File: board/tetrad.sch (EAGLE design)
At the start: 92 parts, among them J2 CONN-03X2-MICROFIT-430450612, Q1 FET-PCH-TO252, Q10 FET-NCH-SOT23, Q11 FET-NCH-SOT23, Q12 FET-NCH-SOT23, Q2 FET-NCH-SOT23, Q3 FET-NCH-SOT23, Q4 FET-NCH-SOT23, Q5 FET-NCH-SOT23, Q6 FET-NCH-SOT23, Q7 FET-NCH-SOT23, Q8 FET-NCH-SOT23, Q9 FET-NCH-SOT23, U1 IO-MCP23017SO, U2 RADIO-ESP32_DEVKIT, U3 R-78E5.0-1.0

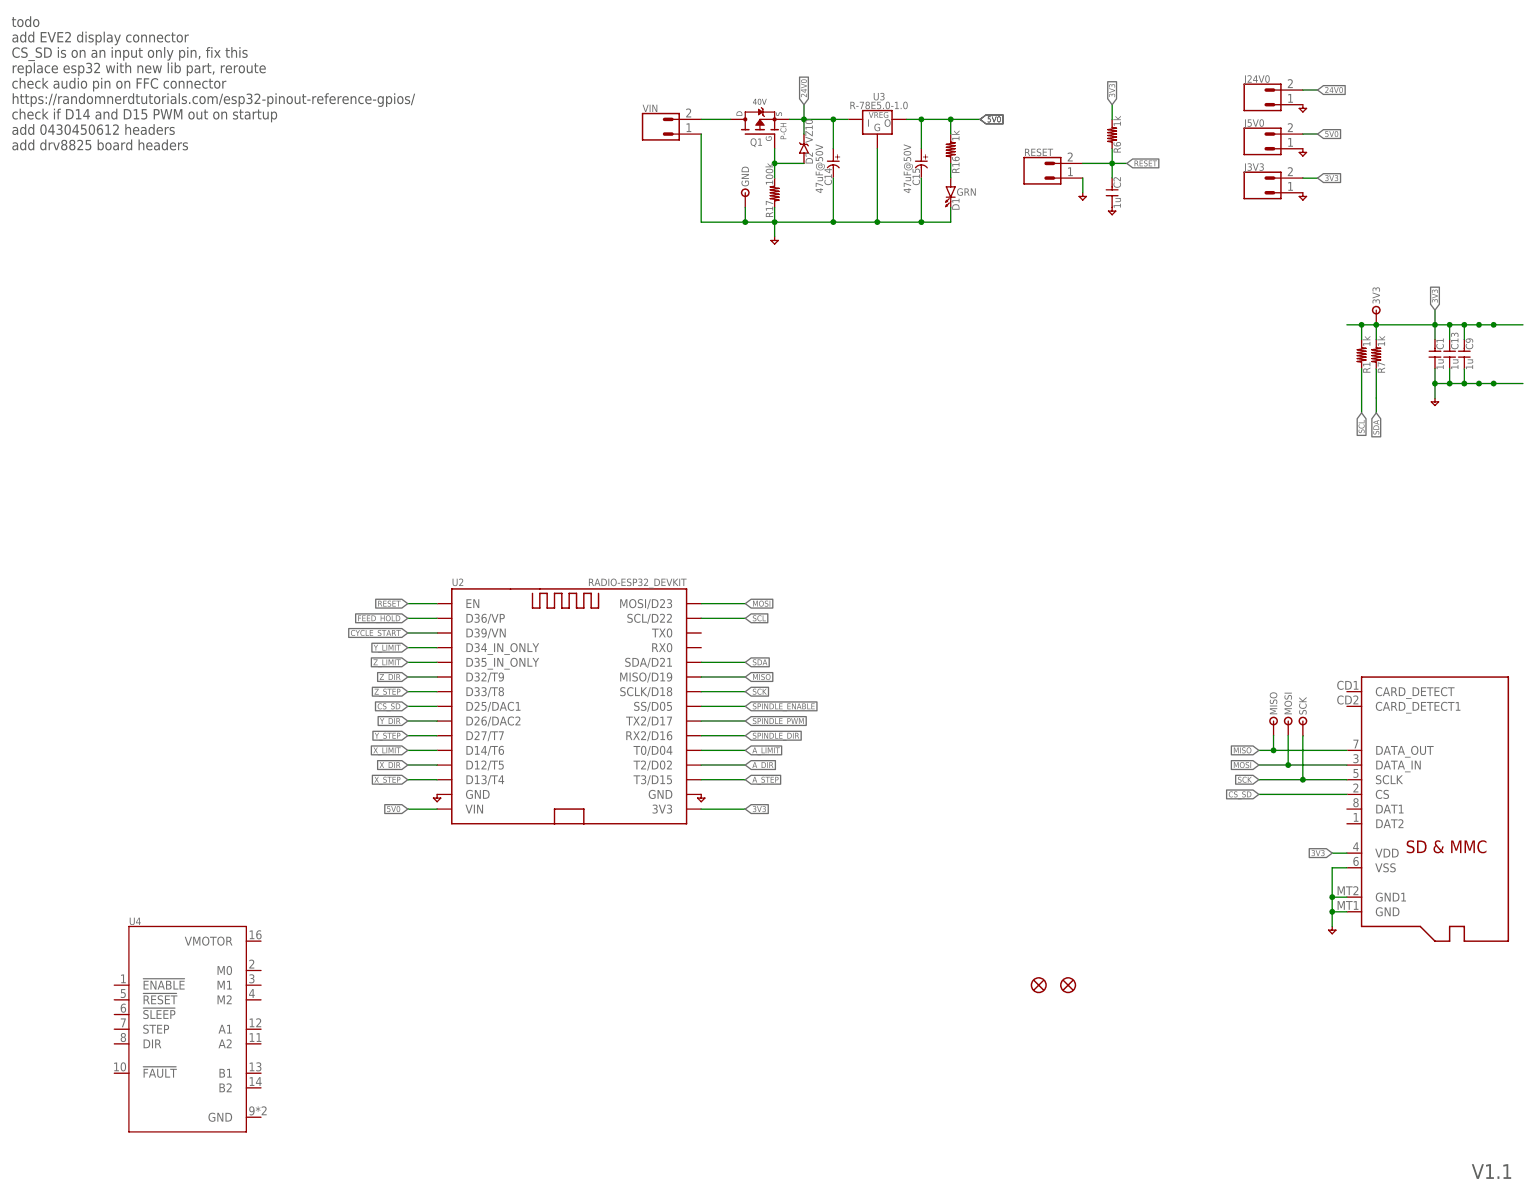
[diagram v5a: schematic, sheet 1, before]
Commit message: selected hammond enclosure and larger board
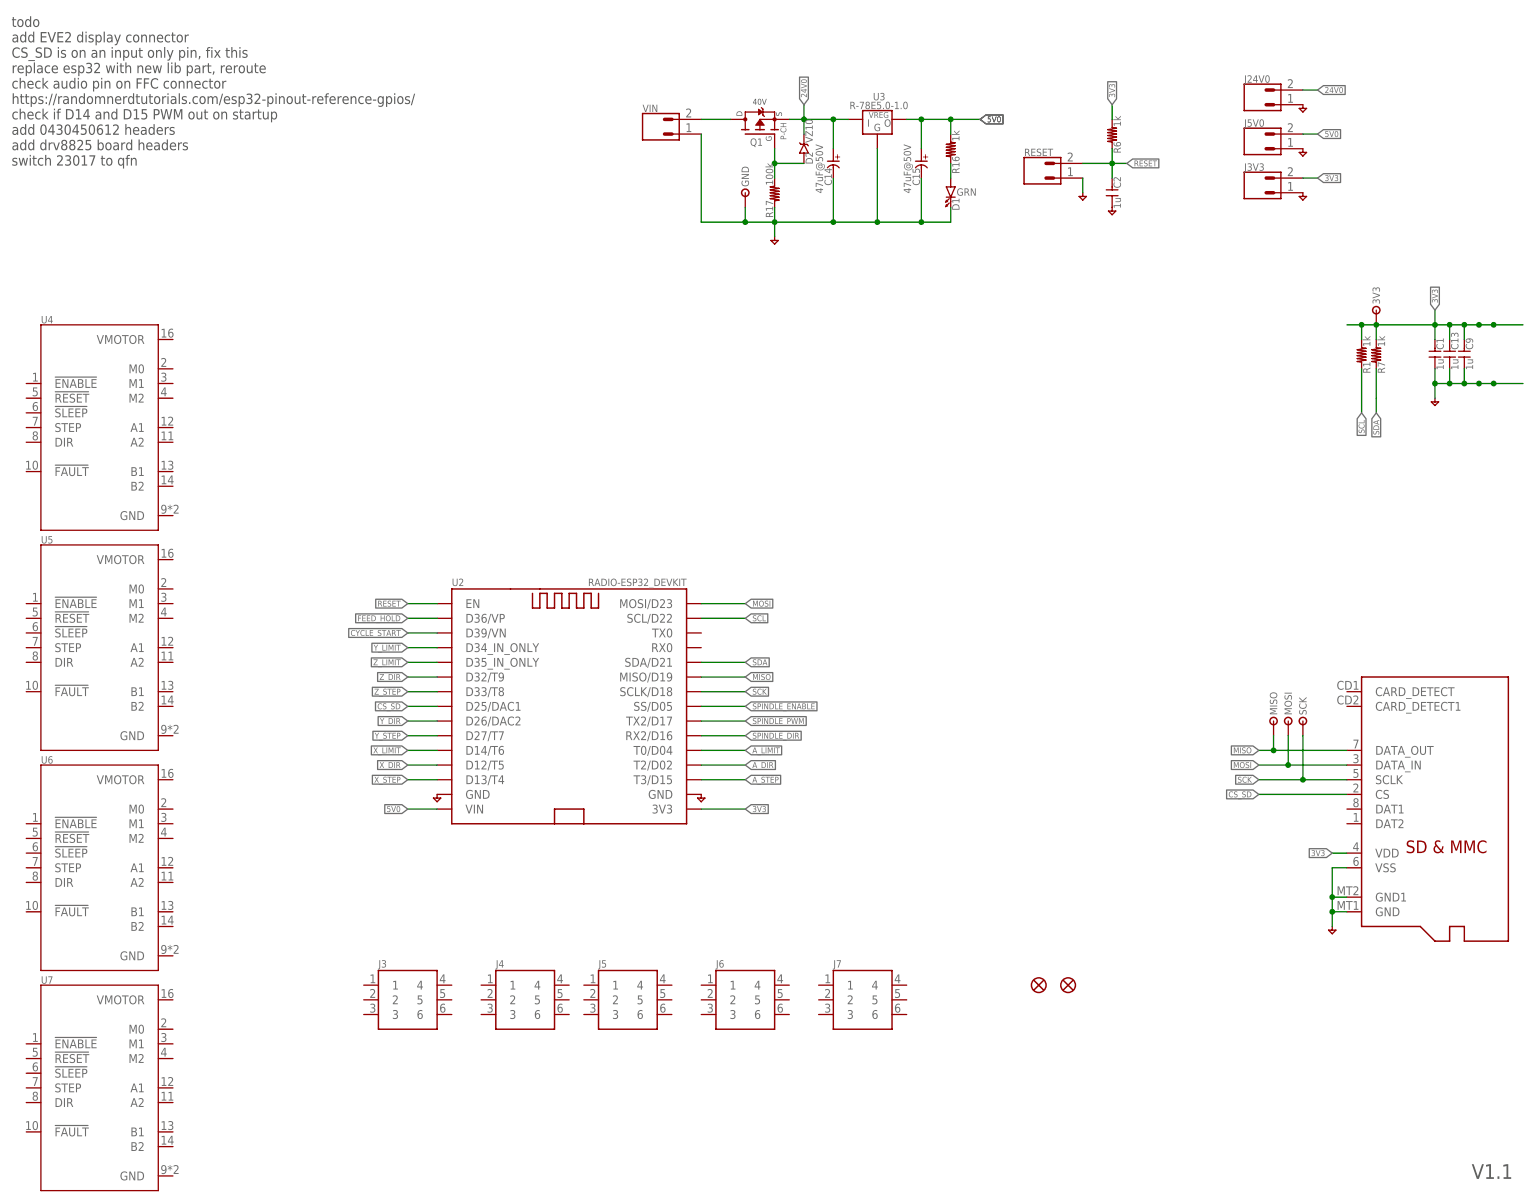
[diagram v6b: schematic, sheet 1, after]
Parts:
- added J3, J4, J5, J6, J7: (no value), holla:CONN-03X2-MICROFIT-430450612
- added U5, U6, U7: (no value), holla:BOARD-DRV8825-CARRIER
- J2: value CONN-03X2-MICROFIT-430450612 -> (none)
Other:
- note added: "todo add EVE2 display connector CS_SD is on an input only pin, fix this replace esp32 with new lib part, reroute check audio pin on FFC connector https://randomnerdtutorials.com/esp32-pinout-reference-gpios/ check if D14 and D15 PWM out on startup add 0430450612 headers add drv8825 board headers switch 23017 to qfn"
- note removed: "todo add EVE2 display connector CS_SD is on an input only pin, fix this replace esp32 with new lib part, reroute check audio pin on FFC connector https://randomnerdtutorials.com/esp32-pinout-reference-gpios/ check if D14 and D15 PWM out on startup add 0430450612 headers add drv8825 board headers"
- moved on the sheet: U4
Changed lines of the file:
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@@
 <part name="J2" library="holla" deviceset="CONN-03X2-MICROFIT" device="-430450612"/>
 <part name="U4" library="holla" deviceset="BOARD-DRV8825-CARRIER" device=""/>
+<part name="J3" library="holla" deviceset="CONN-03X2-MICROFIT" device="-430450612"/>
+<part name="J4" library="holla" deviceset="CONN-03X2-MICROFIT" device="-430450612"/>
+<part name="J5" library="holla" deviceset="CONN-03X2-MICROFIT" device="-430450612"/>
+<part name="J6" library="holla" deviceset="CONN-03X2-MICROFIT" device="-430450612"/>
+<part name="J7" library="holla" deviceset="CONN-03X2-MICROFIT" device="-430450612"/>
+<part name="U5" library="holla" deviceset="BOARD-DRV8825-CARRIER" device=""/>
+<part name="U6" library="holla" deviceset="BOARD-DRV8825-CARRIER" device=""/>
+<part name="U7" library="holla" deviceset="BOARD-DRV8825-CARRIER" device=""/>
 </parts>
 <sheets>
@@
 check if D14 and D15 PWM out on startup
 add 0430450612 headers
-add drv8825 board headers</text>
+add drv8825 board headers
+switch 23017 to qfn</text>
 <text x="138.43" y="193.04" size="1.016" layer="97">40V</text>
 <text x="262.89" y="7.112" size="2.54" layer="97">V1.1</text>
@@
 <instance part="RESET" gate="G$1" x="190.5" y="180.34"/>
 <instance part="U2" gate="G$1" x="106.68" y="88.9"/>
-<instance part="U4" gate="G$1" x="40.64" y="33.02"/>
+<instance part="U4" gate="G$1" x="25.4" y="137.16"/>
+<instance part="J3" gate="G$1" x="78.74" y="38.1"/>
+<instance part="J4" gate="G$1" x="99.06" y="38.1"/>
+<instance part="J5" gate="G$1" x="116.84" y="38.1"/>
+<instance part="J6" gate="G$1" x="137.16" y="38.1"/>
+<instance part="J7" gate="G$1" x="157.48" y="38.1"/>
+<instance part="U5" gate="G$1" x="25.4" y="99.06"/>
+<instance part="U6" gate="G$1" x="25.4" y="60.96"/>
+<instance part="U7" gate="G$1" x="25.4" y="22.86"/>
 </instances>
 <busses>

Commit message: started initial positioning
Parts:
- J2, J3, J4, J5, J6, J7: device holla:CONN-03X2-MICROFIT-430450612 -> holla:CONN-03X2-MICROFIT-TH-SMD
- U1: value IO-MCP23017SO -> IO-MCP23017ML; device holla:IO-MCP23017SO -> holla:IO-MCP23017ML
- U4, U5, U6, U7: device holla:BOARD-DRV8825-CARRIER -> holla:BOARD-DRV8825-CARRIER-TH-SMD

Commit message: started placement of X
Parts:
- removed J3, J4, J5, J6: (no value), holla:CONN-03X2-MICROFIT-TH-SMD
- removed U4, U5, U6, U7: (no value), holla:BOARD-DRV8825-CARRIER-TH-SMD
- added C16: 47u, holla:C-1206
- added R28, R30, R32, R34, R36, R38, R40, R42, R44, R46, R48, R50, R52, R54, R56, R58: 0, holla:R-0603
- added R37, R39, R41, R43, R45, R47, R49, R51, R53, R55, R57, R59, RXM0, RXM1, RXM2: DNP, holla:R-0603
- added UA, UX, UY, UZ: (no value), holla:BOARD-DRV8825-CARRIER-TH-SMD
- A, X, Y, Z: device holla:CONN-06-.100-VERT-HEADER -> holla:CONN-03X2-MICROFIT-TH-SMD
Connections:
- removed net X_STEP_5V0: Q12.D, X.3
- new net AA1: UA.A1
- new net AA2: UA.A2
- new net AB1: UA.B1
- new net AB2: UA.B2
- new net N$21: Q12.D, R32.2, UX.STEP
- new net N$25: R34.2, UX.A2, X.6
- new net N$30: R28.1, UX.A1, X.3
- new net N$31: R32.1, UX.B1, X.2
- new net N$32: R30.1, UX.B2, X.1
- new net N$33: RXM0.1, UX.M0
- new net N$34: RXM1.1, UX.M1
- new net N$35: RXM2.1, UX.M2
- new net YA1: UY.A1
- new net YA2: UY.A2
- new net YB1: UY.B1
- new net YB2: UY.B2
- new net ZA1: UZ.A1
- new net ZA2: UZ.A2
- new net ZB1: UZ.B1
- new net ZB2: UZ.B2
- net 24V0: now also C16.1, R28.2, UA.VMOTOR, UX.VMOTOR, UY.VMOTOR, UZ.VMOTOR; no longer A.6, X.6, Y.6, Z.6
- net 3V3: now also RXM0.2, RXM1.2, RXM2.2, UX.!RESET, UX.!SLEEP
- net 5V0: now also A.1, R30.2, UX.!FAULT, Y.1, Z.1; no longer A.5, X.5, Y.5, Z.5
- net GND: now also A.4, C16.2, UA.GND, UX.GND, UX.VMGND, UY.GND, UZ.GND, X.4, Y.4, Z.4; no longer A.1, X.1, Y.1, Z.1
- net N$10: no longer A.4
- net N$11: no longer A.2
- net N$2: now also X.5; no longer X.4
- net N$5: now also R34.1, UX.DIR; no longer X.2
- net N$6: no longer Y.4
- net N$7: no longer Y.2
- net N$8: no longer Z.4
- net N$9: no longer Z.2
- net X_STEP_5V1: no longer Y.3
- net X_STEP_5V2: no longer Z.3
- net X_STEP_5V3: no longer A.3
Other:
- moved on the sheet: C10, C11, C4, C6, Q11, Q12, Q2, Q3, Q4, Q5, Q6, Q7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
